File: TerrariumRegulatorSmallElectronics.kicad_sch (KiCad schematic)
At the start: 50 parts, among them J101 Conn_01x03, J102 Barrel_Jack, J103 Conn_01x03, J104 USB_B_Micro, J105 jtag, J106 Conn_01x02, J107 Conn_01x02, SW101 SW_Push, SW102 SW_Push, SW103 SW_Push, SW104 SW_Push, SW105 SW_Push, U101 LTC1174CS8_PBF, U102 STM32F103RBTx, U103 L298N, U104 ST7735, Y101 Crystal

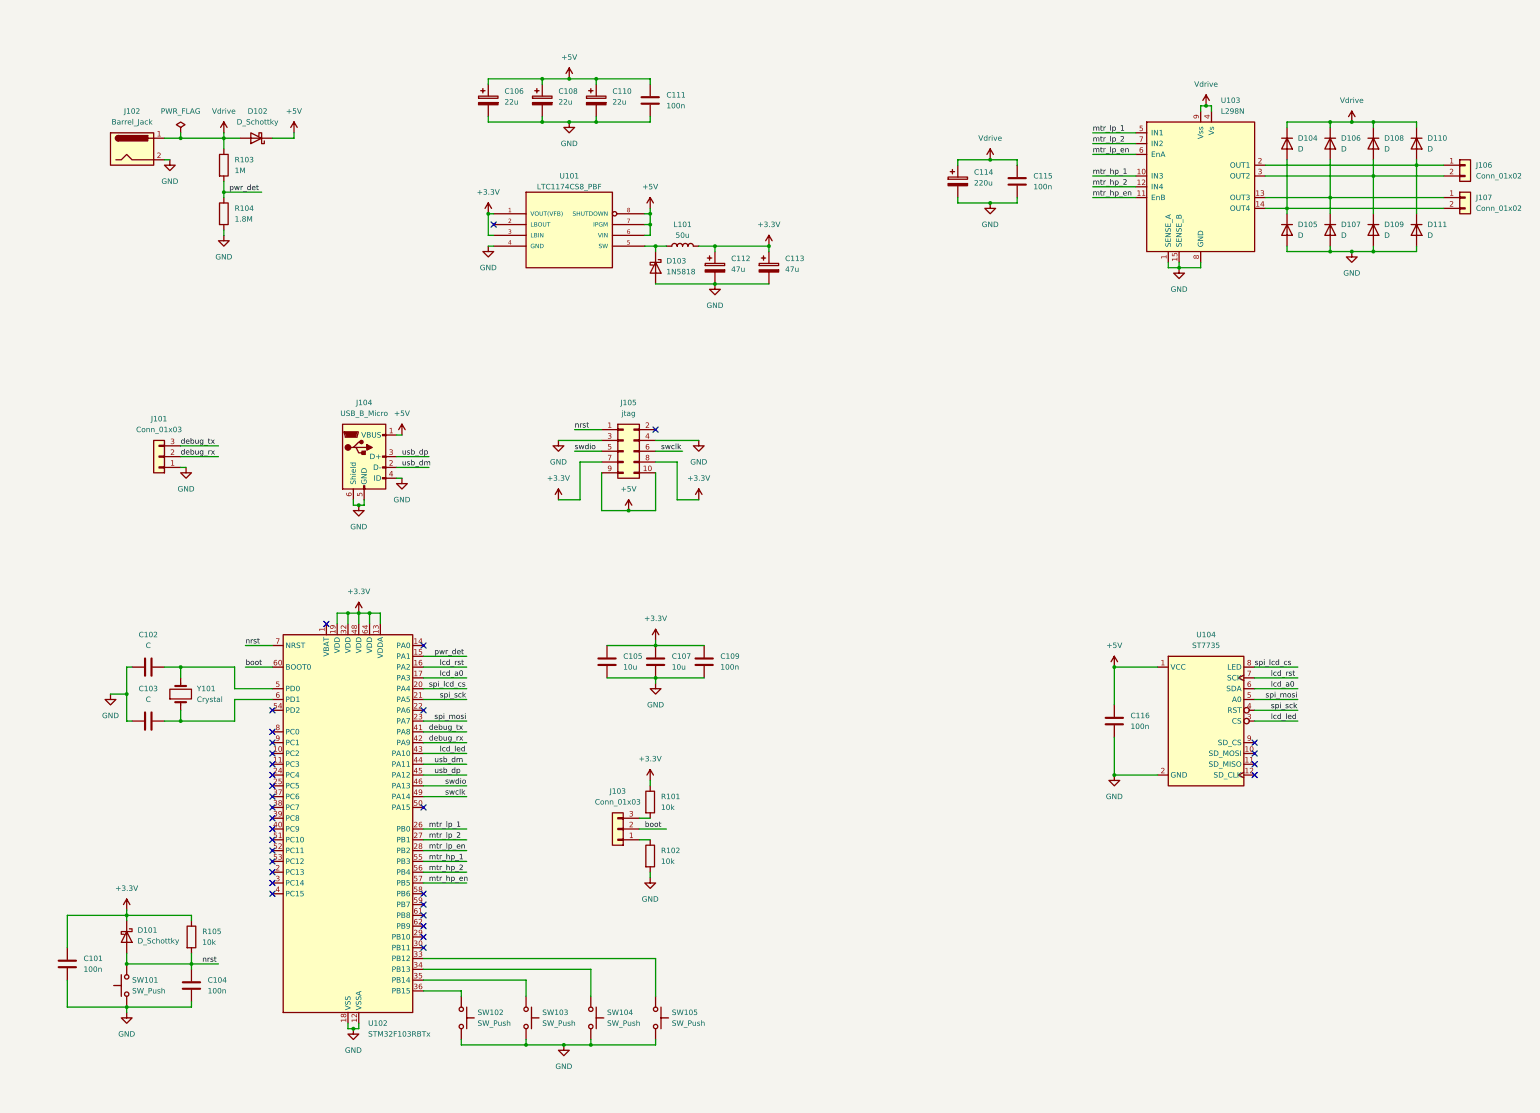
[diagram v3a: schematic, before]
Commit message: Added sensor matrix and fixed debug header pinout
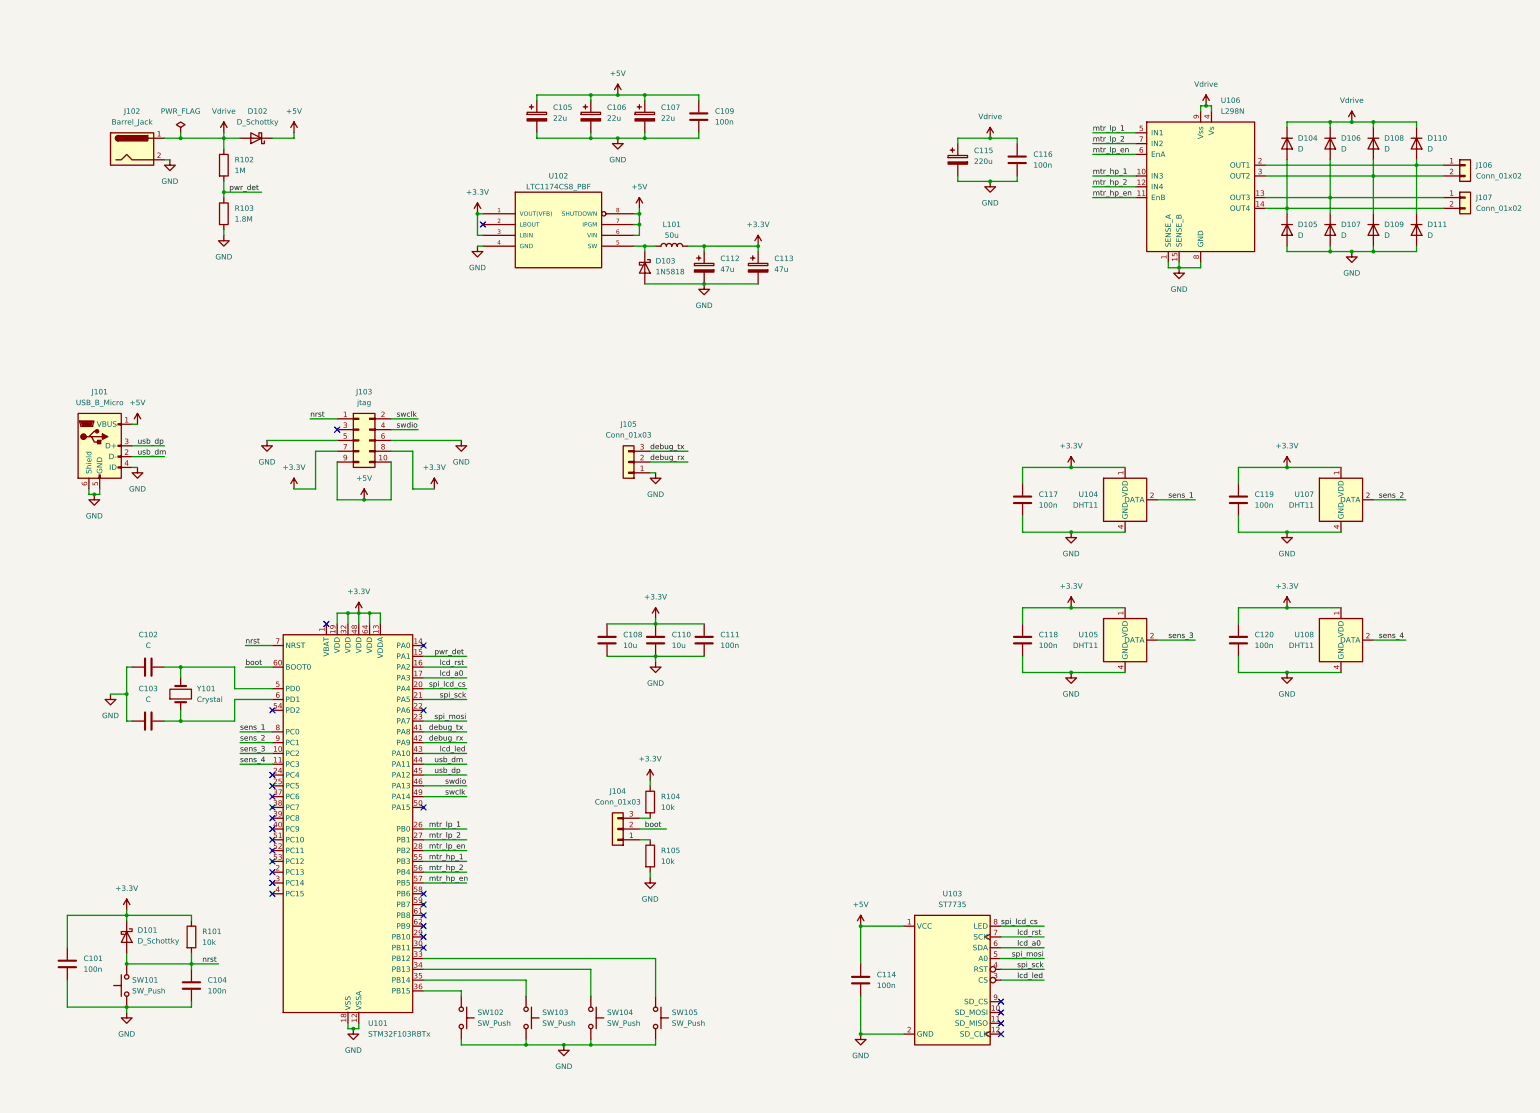
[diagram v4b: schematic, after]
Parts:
- added C117, C118, C119, C120: 100n, symbol Device:C
- added U104, U105, U107, U108: DHT11, Sensor:Aosong_DHT11_5.5x12.0_P2.54mm, symbol Sensor:DHT11
- renumbered C106 to C105, C108 to C106, C110 to C107, C105 to C108, C111 to C109, C107 to C110, C109 to C111, C116 to C114, C114 to C115, C115 to C116, J104 to J101, J105 to J103, J103 to J104, J101 to J105, R105 to R101, R103 to R102, R104 to R103, R101 to R104, R102 to R105, U102 to U101, U101 to U102, U104 to U103, U103 to U106
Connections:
- net +3.3V: now also C117.1, C118.1, C119.1, C120.1, U104.1 (VDD), U105.1 (VDD), U107.1 (VDD), U108.1 (VDD)
- net GND: now also J103.5 (Pin_5), J103.6 (Pin_6), C117.2, C118.2, C119.2, C120.2, U104.4 (GND), U105.4 (GND), U107.4 (GND), U108.4 (GND); no longer J103.3 (Pin_3), J103.4 (Pin_4)
- net swclk: now also J103.2 (Pin_2); no longer J103.6 (Pin_6)
- net swdio: now also J103.4 (Pin_4); no longer J103.5 (Pin_5)
- net sens_3: now reaches U101.10 (PC2)
- net sens_3: now also U105.2 (DATA)
- net sens_4: now reaches U101.11 (PC3)
- net sens_4: now also U108.2 (DATA)
- net sens_1: now reaches U101.8 (PC0)
- net sens_1: now also U104.2 (DATA)
- net sens_2: now reaches U101.9 (PC1)
- net sens_2: now also U107.2 (DATA)
- no-connect marks 33 -> 29
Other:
- moved on the sheet: C105, C106, C107, C108, C109, C110, C111, C112, C113, C114, C115, C116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
